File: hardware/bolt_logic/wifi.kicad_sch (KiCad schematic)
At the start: 7 parts, among them J4 ESP PROG, U30 ESP32-WROOM-32UE

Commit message: Revert "Schematic: ESP32-WROOM-32UE (u.FL) instead of WROOM-32"
This reverts commit fcac408. The WiFi stays as on the Tesla V6 board
(PCB-antenna module); the change was not requested by the owner, and the
housing will be handled separately.

Co-Authored-By: Claude Opus 5.5 <noreply@anthropic.com>
Claude-Session: https://claude.ai/code/session_01KW1M8KfVLc83FDDiK2YEWM
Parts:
- U30: value ESP32-WROOM-32UE -> ESP32-WROOM-32; footprint RF_Module:ESP32-WROOM-32UE -> RF_Module:ESP32-WROOM-32; symbol RF_Module:ESP32-WROOM-32UE -> RF_Module:ESP32-WROOM-32
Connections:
- no-connect marks 23 -> 29
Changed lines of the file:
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@@
     (at 58.42 63.5)
+)
+  (no_connect
+    (at 27.94 81.28)
+)
+  (no_connect
+    (at 27.94 83.82)
+)
+  (no_connect
+    (at 27.94 88.9)
 )
   (wire
@@
         (font (size 1.27 1.27)) hide)))
   (no_connect
+    (at 27.94 86.36)
+)
+  (no_connect
+    (at 27.94 76.2)
+)
+  (no_connect
+    (at 27.94 78.74)
+)
+  (no_connect
     (at 58.42 68.58)
 )
@@
         (font (size 1.27 1.27)) hide)))
   (symbol
-    (lib_id "RF_Module:ESP32-WROOM-32UE")
+    (lib_id "RF_Module:ESP32-WROOM-32")
     (at 43.18 76.2 0)
     (unit 1)
@@
         (font (size 1.27 1.27))
         (justify left)))
-    (property "Value" "ESP32-WROOM-32UE"
+    (property "Value" "ESP32-WROOM-32"
       (at 27.94 114.16 0)
       (effects
         (font (size 1.27 1.27))
         (justify left)))
-    (property "Footprint" "RF_Module:ESP32-WROOM-32UE"
+    (property "Footprint" "RF_Module:ESP32-WROOM-32"
       (at 43.18 76.2 0)
       (effects

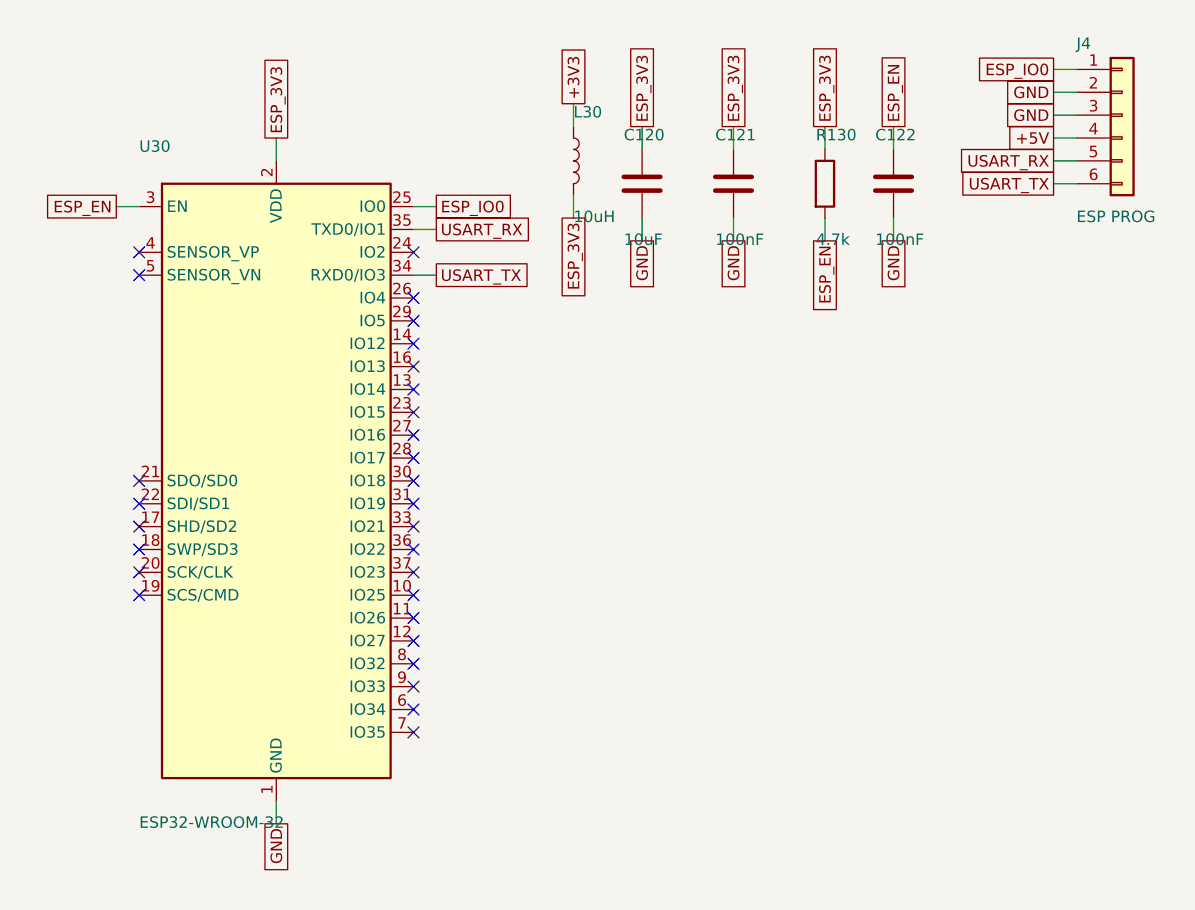
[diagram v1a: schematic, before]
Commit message: Schematic: WiFi matches Tesla V6 IC14 exactly
- U30 value ESP32-WROOM-32E (M113EH2800PH3Q0, PCB antenna), the V6 part;
  same land pattern as the WROOM-32 footprint.
- 100 nF moved to the 3.3 V side of the 10 uH inductor, as V6 C11
  (10 uF stays on the module side, as C65). Netlist re-verified.

Co-Authored-By: Claude Opus 5.5 <noreply@anthropic.com>
Claude-Session: https://claude.ai/code/session_01KW1M8KfVLc83FDDiK2YEWM
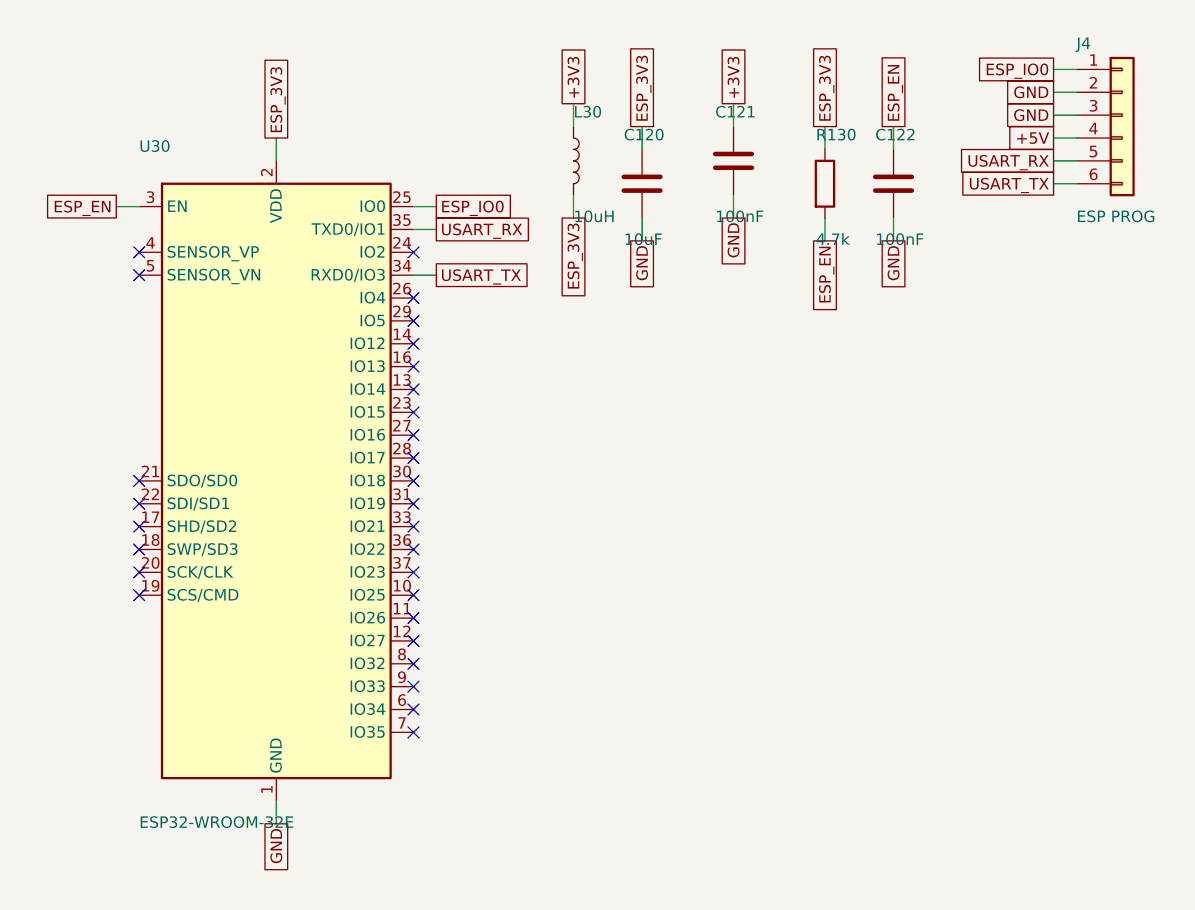
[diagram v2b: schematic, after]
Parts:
- U30: value ESP32-WROOM-32 -> ESP32-WROOM-32E
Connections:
- net +3V3: now also C121.1
- net ESP_3V3: no longer C121.1
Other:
- moved on the sheet: C121
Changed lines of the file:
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@@
   (wire
     (pts
-      (xy 93.98 39.37)
-      (xy 93.98 36.83))
-    (stroke
-      (width 0)
-      (type default))
-)
-  (global_label "ESP_3V3"
-    (shape passive)
-    (at 93.98 36.83 90)
+      (xy 93.98 36.83)
+      (xy 93.98 34.29))
+    (stroke
+      (width 0)
+      (type default))
+)
+  (global_label "+3V3"
+    (shape passive)
+    (at 93.98 34.29 90)
     (fields_autoplaced)
     (effects
@@
       (justify left))
     (property "Intersheetrefs" "${INTERSHEET_REFS}"
-      (at 93.98 36.83 0)
-      (effects
-        (font (size 1.27 1.27)) hide)))
-  (wire
-    (pts
-      (xy 93.98 46.99)
-      (xy 93.98 49.53))
+      (at 93.98 34.29 0)
+      (effects
+        (font (size 1.27 1.27)) hide)))
+  (wire
+    (pts
+      (xy 93.98 44.45)
+      (xy 93.98 46.99))
     (stroke
       (width 0)
@@
   (global_label "GND"
     (shape passive)
-    (at 93.98 49.53 270)
-    (fields_autoplaced)
-    (effects
-      (font (size 1.27 1.27))
-      (justify right))
-    (property "Intersheetrefs" "${INTERSHEET_REFS}"
-      (at 93.98 49.53 0)
+    (at 93.98 46.99 270)
+    (fields_autoplaced)
+    (effects
+      (font (size 1.27 1.27))
+      (justify right))
+    (property "Intersheetrefs" "${INTERSHEET_REFS}"
+      (at 93.98 46.99 0)
       (effects
         (font (size 1.27 1.27)) hide)))
@@
         (font (size 1.27 1.27))
         (justify left)))
-    (property "Value" "ESP32-WROOM-32"
+    (property "Value" "ESP32-WROOM-32E"
       (at 27.94 114.16 0)
       (effects
@@
   (symbol
     (lib_id "Device:C")
-    (at 93.98 43.18 0)
+    (at 93.98 40.64 0)
     (unit 1)
     (in_bom yes)
@@
     (dnp no)
     (property "Reference" "C121"
-      (at 91.948 37.77 0)
+      (at 91.948 35.23 0)
       (effects
         (font (size 1.27 1.27))
         (justify left)))
     (property "Value" "100nF"
-      (at 91.948 49.39 0)
+      (at 91.948 46.85 0)
       (effects
         (font (size 1.27 1.27))
         (justify left)))
     (property "Footprint" "Capacitor_SMD:C_0805_2012Metric"
-      (at 93.98 43.18 0)
+      (at 93.98 40.64 0)
       (effects
         (font (size 1.27 1.27)) hide))
     (property "Datasheet" "~"
-      (at 93.98 43.18 0)
-      (effects
-        (font (size 1.27 1.27)) hide))
+      (at 93.98 40.64 0)
+      (effects
+        (font (size 1.27 1.27)) hide))
